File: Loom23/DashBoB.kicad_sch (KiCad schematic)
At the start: 0 parts

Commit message: Added paddle shifter PCB and the relays.
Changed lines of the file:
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@@
-    (effects (font (size 1.27 1.27)) (justify left))
-  )
-  (hierarchical_label "I2C (SDA) (E)" (shape input) (at 172.72 113.03 0)
     (effects (font (size 1.27 1.27)) (justify left))
   )
@@
     (effects (font (size 1.27 1.27)) (justify left))
   )
-  (hierarchical_label "I2C (SCL)" (shape input) (at 148.59 72.39 90)
-    (effects (font (size 1.27 1.27)) (justify left))
-  )
-  (hierarchical_label "I2C (SDA)" (shape input) (at 151.13 72.39 90)
-    (effects (font (size 1.27 1.27)) (justify left))
-  )
-  (hierarchical_label "Paddle shift neutral (E)" (shape input) (at 172.72 123.19 0)
+  (hierarchical_label "NeutralSignal(E)" (shape input) (at 172.72 123.19 0)
     (effects (font (size 1.27 1.27)) (justify left))
   )
@@
     (effects (font (size 1.27 1.27)) (justify left))
   )
-  (hierarchical_label "I2C (SCL) (E)" (shape input) (at 172.72 115.57 0)
-    (effects (font (size 1.27 1.27)) (justify left))
-  )

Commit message: Added brake light
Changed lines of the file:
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@@
+    (effects (font (size 1.27 1.27)) (justify left))
+  )
+  (hierarchical_label "CANL" (shape input) (at 172.72 115.57 0)
     (effects (font (size 1.27 1.27)) (justify left))
   )
@@
     (effects (font (size 1.27 1.27)) (justify left))
   )
+  (hierarchical_label "CANH" (shape input) (at 172.72 113.03 0)
+    (effects (font (size 1.27 1.27)) (justify left))
+  )

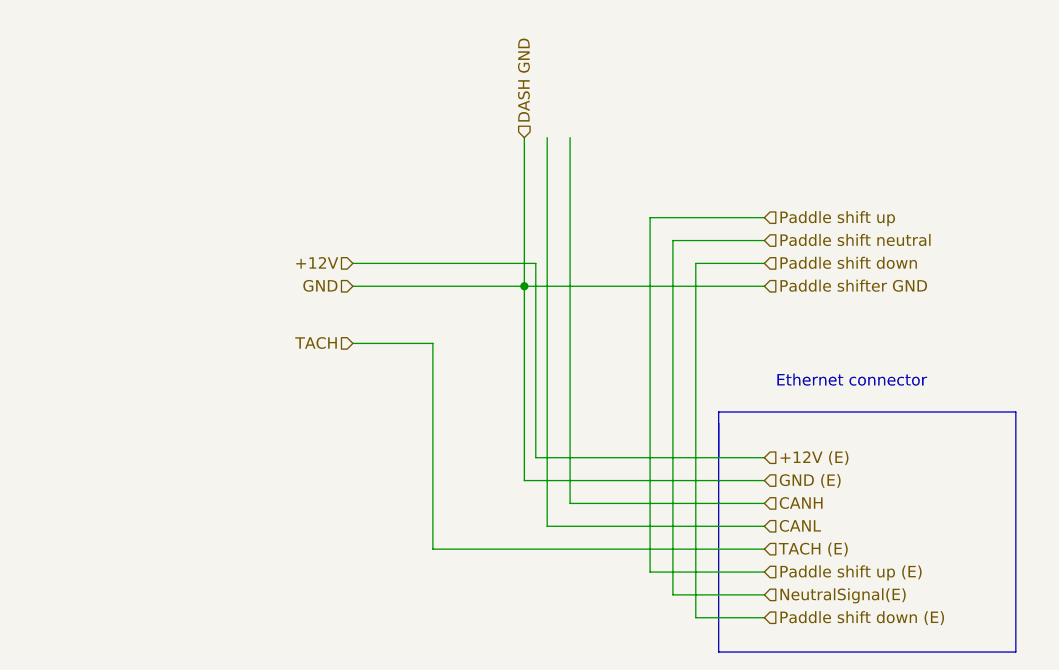
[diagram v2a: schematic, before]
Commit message: Changed labels to match old wires
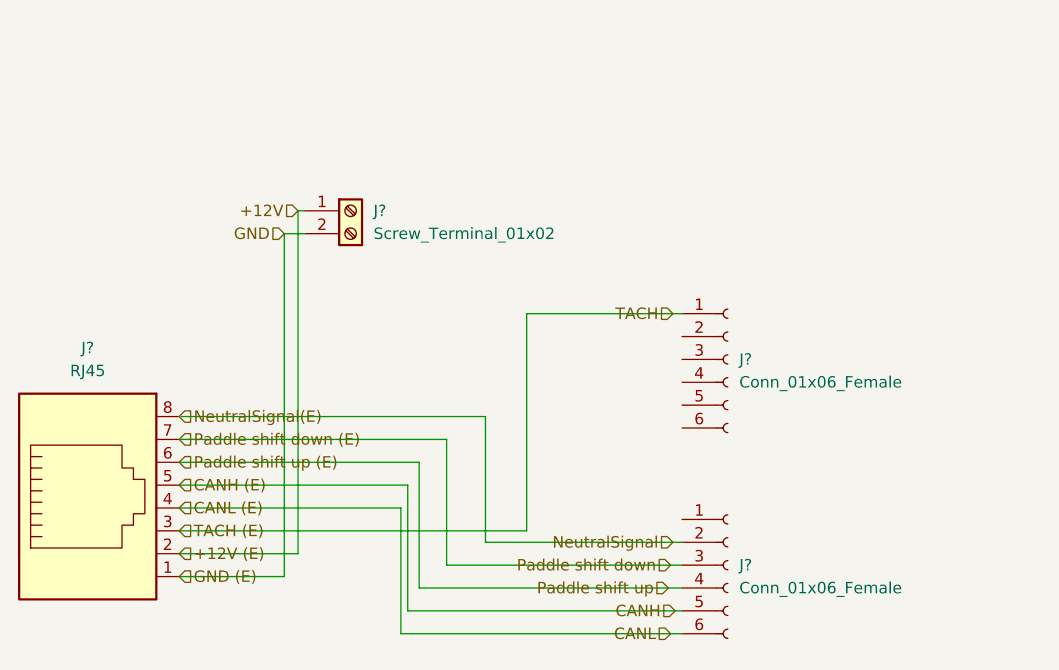
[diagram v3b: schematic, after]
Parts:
- added J?: RJ45, Footprints:RJ45_TE_5557789-1, symbol Connector:RJ45
- added J? (x2): Conn_01x06_Female, Footprints:JST_XA_B06B-XASK-1_1x06_P2.50mm_Vertical, symbol Connector:Conn_01x06_Female
- added J?: Screw_Terminal_01x02, TerminalBlock:TerminalBlock_bornier-2_P5.08mm, symbol Connector:Screw_Terminal_01x02
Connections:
- net +12V: now also J?.1 (Pin_1), J?.2
- net CANH: now also J?.5, J?.5 (Pin_5)
- net CANL: now also J?.4, J?.6 (Pin_6)
- net NeutralSignal(E): now also J?.8
- net Paddle shift down: now also J?.3 (Pin_3), J?.7
- net Paddle shift up: now also J?.4 (Pin_4), J?.6
- net TACH: now also J?.1 (Pin_1), J?.3
- new net GND: J?.1, J?.2 (Pin_2)
- new net NeutralSignal: J?.2 (Pin_2)
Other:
- note removed: "Ethernet connector"
